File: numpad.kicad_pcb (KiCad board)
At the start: 2 copper layers, 90 x 132.2 mm, 162 parts, among them J1 TYPE-C_16PIN_2MD(073), J2 Header-2_54_1x3, SW1 TS-1187A-B-A-B, SW2 TS-1187A-B-A-B, U1 LM3940IMP-3_3/NOPB, U2 RP2040, U3 128Mbit, U4 SN74LV1T34DBVR, Y1 ABM8-272-T3_C20625731

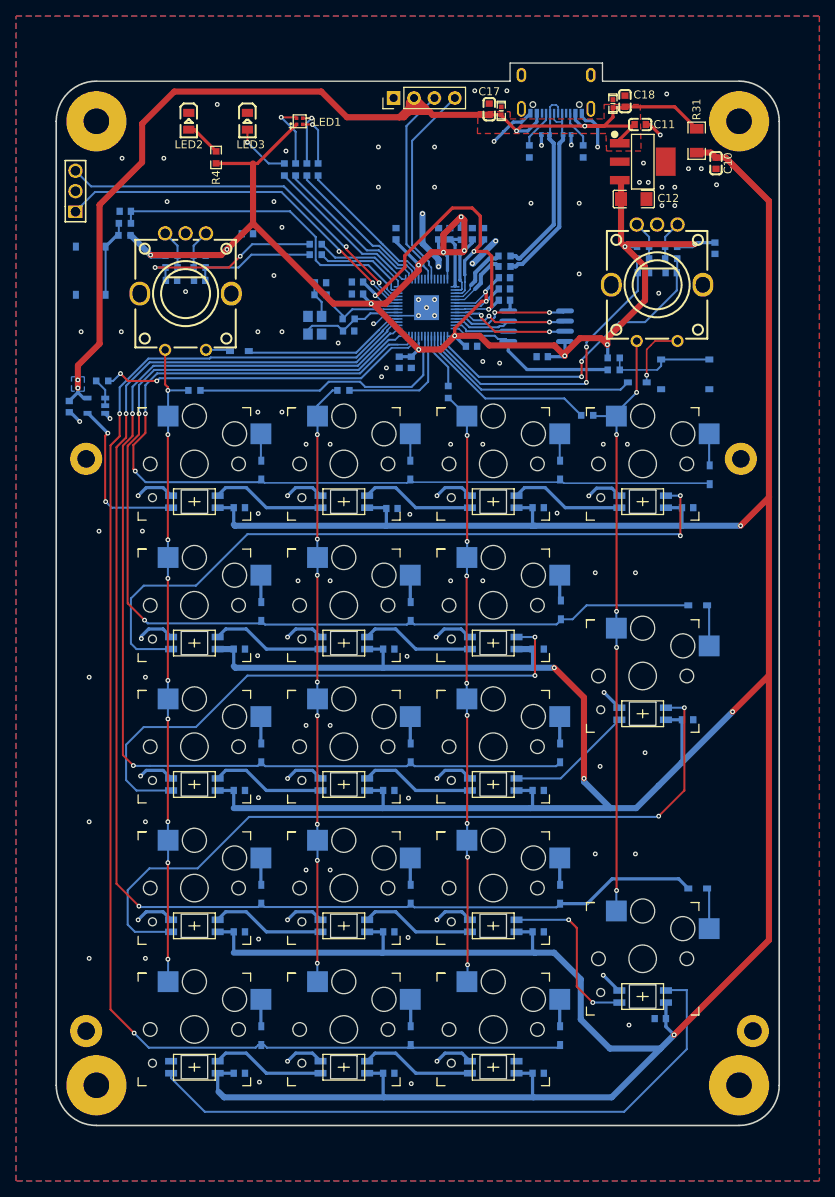
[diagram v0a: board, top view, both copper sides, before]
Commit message: Added silkscreen details
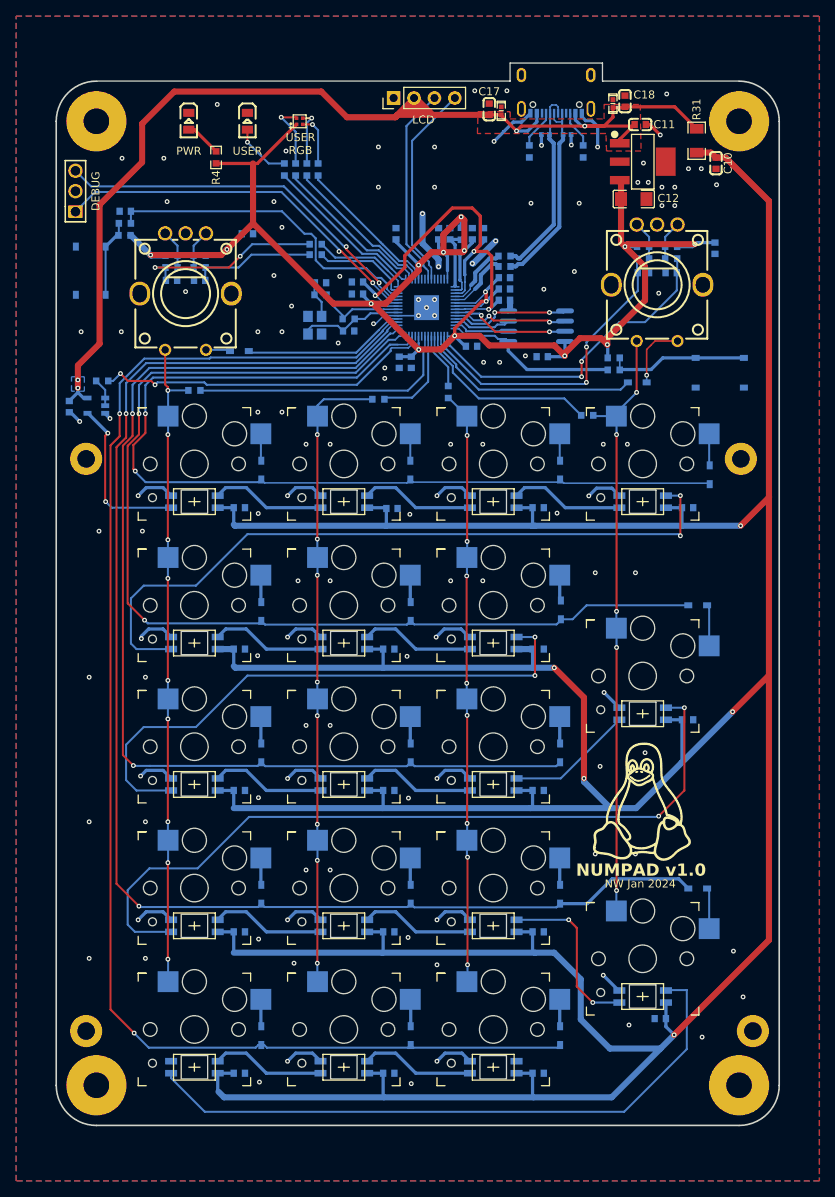
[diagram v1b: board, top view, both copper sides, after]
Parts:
- added G***: LOGO, LOGO, F.Cu at (117.9, 124.7)
- USER RGB: renamed from LED1
- moved R9 4.49 mm to (85.1, 74.6)
- moved SW2 4.30 mm to (127.6, 71.3)
- renumbered LED2 to PWR, LED3 to USER
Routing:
- net Net-(SW2-C): track 13.7 -> 17.6 mm
- net COL1: track 75.1 -> 79.0 mm
- net /MCU/COL1_R: track 15.9 -> 12.0 mm
- net +5V_USB: track 141.5 -> 143.8 mm
- net /MCU/LED00_RES: track 41.5 -> 42.3 mm
- net /MCU/COL0_R: track 34.0 -> 33.5 mm
- net GND: vias 115 -> 124
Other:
- board text added: "BOOT"
- board text added: "DEBUG"
- board text added: "JLCJLCJLCJLC"
- board text added: "LCD"
- board text added: "NUMPAD v1.0"
- board text added: "NW Jan 2024"
- board text added: "Reset"
- board text added: "USER RGB"
